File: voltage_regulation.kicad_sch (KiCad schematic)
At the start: 24 parts, among them IC3 NCV317BD2TR4G, U1 TPS73601MDRBREP, U2 TPS73601MDRBREP

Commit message: Lots of small changes
Some power and ground planes need to be looked at
All parts need to be reexamined before ordering
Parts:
- removed C21: 10uF, Capacitor_Tantalum_SMD:CP_EIA-7343-31_Kemet-D, symbol Device:C_Polarized
- removed C22: 10uF, Capacitor_SMD:C_1206_3216Metric, symbol Device:C_Small
- removed Cin1, Cin2: 1uF, Capacitor_SMD:C_1206_3216Metric, symbol Device:C_Polarized
- removed D1, D2: 1N4002, Diode_THT:D_DO-41_SOD81_P10.16mm_Horizontal, symbol Diode:1N4002
- removed IC3: NCV317BD2TR4G, SamacSys_Parts:TO254P1420X457-4N, symbol SamacSys_Parts:NCV317BD2TR4G
- removed RP1_1: 165, Resistor_SMD:R_0805_2012Metric, symbol Device:R
- removed RP1_2: 100, Resistor_SMD:R_0805_2012Metric, symbol Device:R
- added C71: 100uF, Capacitor_SMD:C_1206_3216Metric, symbol Device:C_Small
- added C72: 10nF, Capacitor_SMD:C_1206_3216Metric, symbol Device:C_Small
- added C73: 150pF, Capacitor_SMD:C_1206_3216Metric, symbol Device:C_Small
- added C74: 0.1uF, Capacitor_SMD:C_1206_3216Metric, symbol Device:C_Small
- added C75: 1500pF, Capacitor_SMD:C_1206_3216Metric, symbol Device:C_Small
- added C76, C77: 4.7uF, Capacitor_SMD:C_1206_3216Metric, symbol Device:C_Small
- added D1: MBRS340T3G, DIOM8059X261N, symbol SamacSys_Parts:MBRS340T3G
- added IC3: TPS5430DDAR, SOIC127P600X170-9N, symbol SamacSys_Parts:TPS5430DDAR
- added L1: SRP6060FA-150M, SRP6060FA150M, symbol SamacSys_Parts:SRP6060FA-150M
- added R10: 247k, Resistor_SMD:R_1206_3216Metric, symbol Device:R
- added R11: 33k, Resistor_SMD:R_1206_3216Metric, symbol Device:R
- added R7: 10k, Resistor_SMD:R_1206_3216Metric, symbol Device:R
- added R8: 5.9k, Resistor_SMD:R_1206_3216Metric, symbol Device:R
- added R9: 549, Resistor_SMD:R_1206_3216Metric, symbol Device:R
- U1, U2: value TPS73601MDRBREP -> TPS73601MDBVREP; Mouser Part Number 595-TPS73601MDRBREP -> 595-TPS73601MDBVREP; Mouser Price/Stock https://www.mouser.com/ProductDetail/Texas-Instruments/TPS73601MDRBREP?qs=IUbkBnfnSQLnzAa%252BAAvDVA%3D%3D -> https://www.mouser.com/ProductDetail/Texas-Instruments/TPS73601MDBVREP?qs=7kv20MEVUlgO8eFT%2FzKqZA%3D%3D
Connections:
- net +3V3: now also C71.1, C75.2, L1.2, R7.2
- net DC_LINE_IN_28V: now also C76.1, C77.1, IC3.7 (VIN), R10.1
- net GND: now also C71.2, C73.2, C76.2, C77.2, D1.2 (A), IC3.6 (GND), IC3.9 (EP), R11.2, R8.2, R9.2
- new net: C73.1, C74.1, C75.1, IC3.4 (VSENSE), R7.1, R8.1
- new net: C74.2, R9.1
- new net: C72.1, IC3.1 (BOOT)
- new net: C72.2, D1.1 (K), IC3.8 (PH), L1.1
- new net: IC3.5 (ENA), R10.2, R11.1
- no-connect marks 0 -> 3
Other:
- note removed: "NC"
- moved on the sheet: 2V1, 3V0, 3V3, C23, C24, C25, C26, C27, C28, RP2_1, RP2_2, RP3_1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

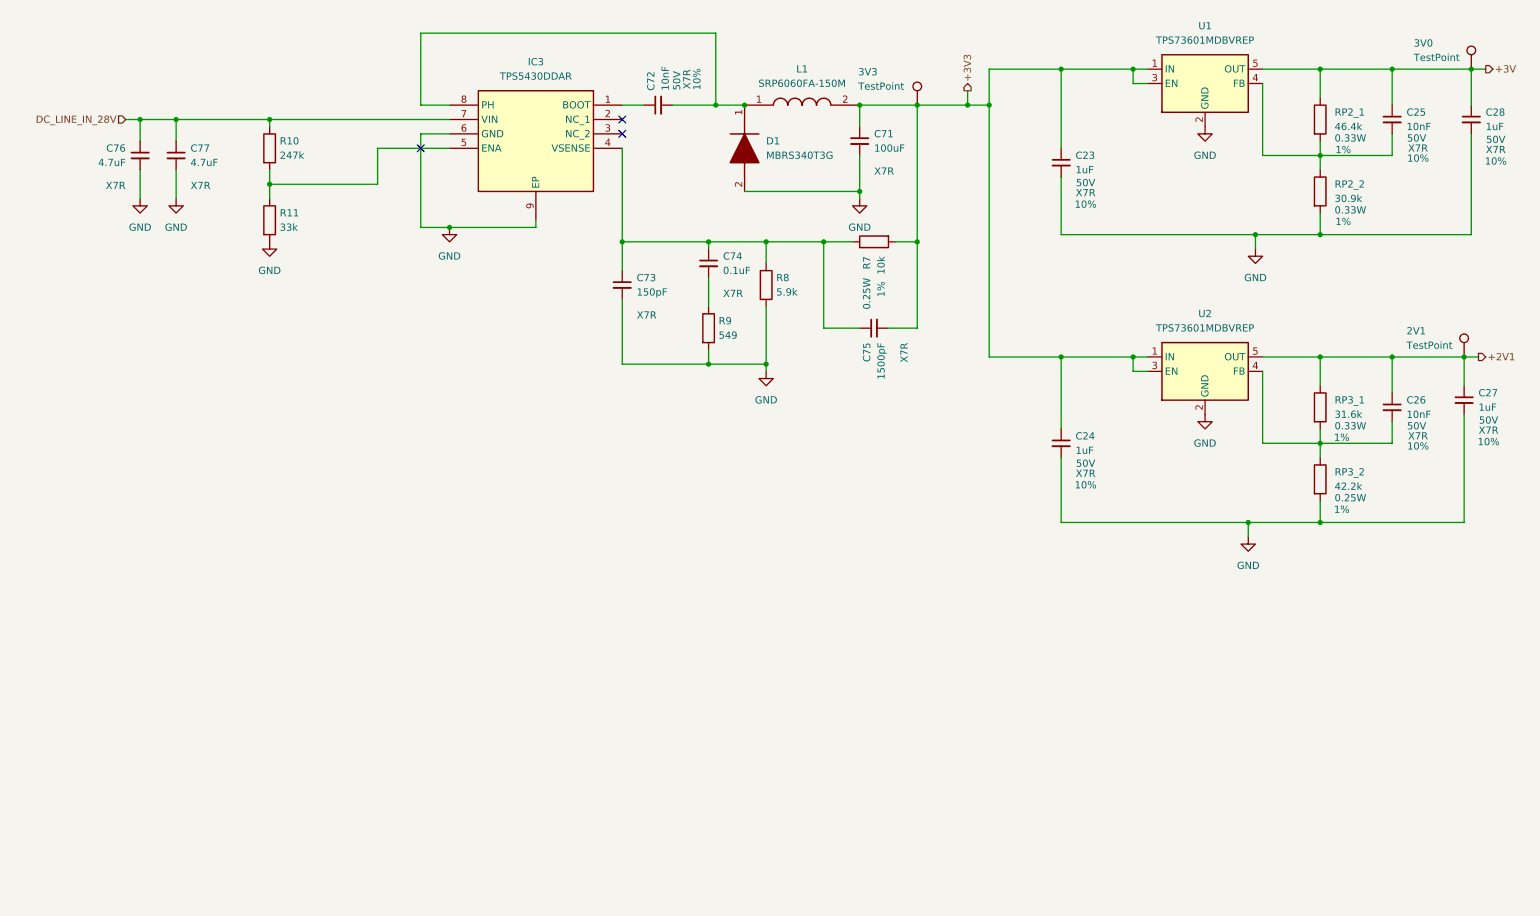
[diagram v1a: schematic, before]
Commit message: Almost done
Taking a break and making a push. Known things to do:
Add pull-up resistors to ETH MDIO, ETH MDC, and XRESL.
Source a 100uF capacitor for primary regulator.
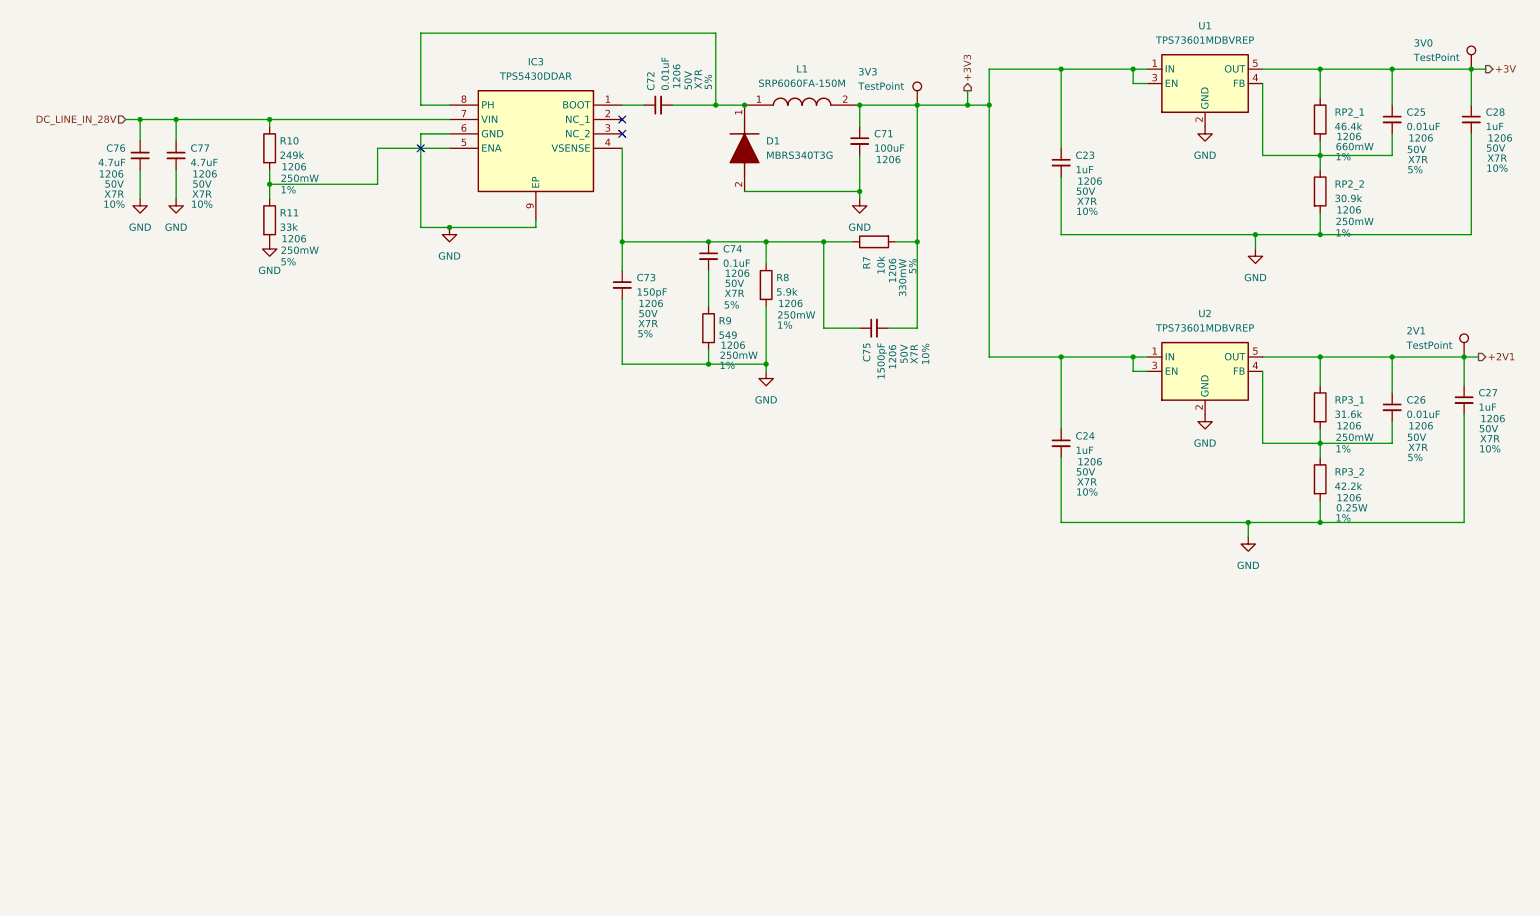
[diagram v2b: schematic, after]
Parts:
- C23, C24, C27, C28: footprint Capacitor_SMD:C_0603_1608Metric -> Capacitor_SMD:C_1206_3216Metric; Mouser Part Number 963-MLASU168AB7105KT -> 963-UMK316B7105KL-T; Mouser Price/Stock https://www.mouser.com/ProductDetail/TAIYO-YUDEN/MLASU168AB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 -> https://www.mouser.com/ProductDetail/TAIYO-YUDEN/UMK316B710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; Package Size (none) -> 1206
- C25, C26: value 10nF -> 0.01uF; footprint Capacitor_SMD:C_0603_1608Metric -> Capacitor_SMD:C_1206_3216Metric; Mouser Part Number 81-GCM188R71H103KA7J -> 581-12065C103J4T4A; Mouser Price/Stock https://www.mouser.com/ProductDetail/Murata-Electronics/GCM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 -> https://www.mouser.com/ProductDetail/KYOCERA-AVX/12065C103J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; Package Size (none) -> 1206; Tolerance 10% -> 5%
- C71: Dielectric X7R -> (none); Mouser Part Number (none) -> Multiple; Mouser Price/Stock (none) -> Multiple; Package Size (none) -> 1206
- C72: value 10nF -> 0.01uF; Mouser Part Number 81-GCM188R71H103KA7J -> 581-12065C103J4T4A; Mouser Price/Stock https://www.mouser.com/ProductDetail/Murata-Electronics/GCM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 -> https://www.mouser.com/ProductDetail/KYOCERA-AVX/12065C103J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; Package Size (none) -> 1206; Tolerance 10% -> 5%
- C73: Mouser Part Number (none) -> 80-C1206C151J5RACTU; Mouser Price/Stock (none) -> https://www.mouser.com/ProductDetail/KEMET/C1206C151J5RACTU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; Package Size (none) -> 1206; Tolerance (none) -> 5%; Voltage Rating (none) -> 50V
- C74: Mouser Part Number (none) -> 581-12065C104J4Z2A; Mouser Price/Stock (none) -> https://www.mouser.com/ProductDetail/KYOCERA-AVX/12065C104J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; Package Size (none) -> 1206; Tolerance (none) -> 5%; Voltage Rating (none) -> 50V
- C75: Mouser Part Number (none) -> 77-VJ1206Y152KXAAC; Mouser Price/Stock (none) -> https://www.mouser.com/ProductDetail/Vishay-Vitramon/VJ1206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; Package Size (none) -> 1206; Tolerance (none) -> 10%; Voltage Rating (none) -> 50V
- C76, C77: Mouser Part Number (none) -> 581-KGM31AR71H475KU; Mouser Price/Stock (none) -> https://www.mouser.com/ProductDetail/KYOCERA-AVX/KGM31AR71H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; Package Size (none) -> 1206; Tolerance (none) -> 10%; Voltage Rating (none) -> 50V
- IC3: Mouser Price/Stock https://www.mouser.co.uk/ProductDetail/Texas-Instruments/TP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 -> https://www.mouser.com/ProductDetail/Texas-Instruments/TPS5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
- R10: value 247k -> 249k; Mouser Part Number (none) -> 71-RCV1206249KFKEA; Mouser Price/Stock (none) -> https://www.mouser.com/ProductDetail/Vishay-Draloric/RCV120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; Package Size (none) -> 1206; Power Rating (none) -> 250mW; Tolerance (none) -> 1%
- R11: Mouser Part Number (none) -> 755-KTR18EZPJ333; Mouser Price/Stock (none) -> https://www.mouser.com/ProductDetail/ROHM-Semiconductor/KTR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; Package Size (none) -> 1206; Power Rating (none) -> 250mW; Tolerance (none) -> 5%
- R7: Mouser Part Number 71-CRCW060310K0FKEI -> 667-ERJ-T08J103V; Mouser Price/Stock https://www.mouser.com/ProductDetail/Vishay-Dale/CRCW060310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 -> https://www.mouser.com/ProductDetail/Panasonic/ERJ-T08J103V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; Package Size (none) -> 1206; Power Rating 0.25W -> 330mW; Tolerance 1% -> 5%
- R8: Mouser Part Number (none) -> 71-CRCW1206-5.9K-E3; Mouser Price/Stock (none) -> https://www.mouser.com/ProductDetail/Vishay-Dale/CRCW12065K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; Package Size (none) -> 1206; Power Rating (none) -> 250mW; Tolerance (none) -> 1%
- R9: Mouser Part Number (none) -> 71-CRCW1206-549-E3; Mouser Price/Stock (none) -> https://www.mouser.com/ProductDetail/Vishay-Dale/CRCW120654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; Package Size (none) -> 1206; Power Rating (none) -> 250mW; Tolerance (none) -> 1%
- RP2_1: footprint Resistor_SMD:R_0603_1608Metric -> Resistor_SMD:R_1206_3216Metric; Mouser Part Number 71-CRCW060346K4FKEAH -> 667-ERJ-P08F4642V; Mouser Price/Stock https://www.mouser.com/ProductDetail/Vishay-Dale/CRCW060346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 -> https://www.mouser.com/ProductDetail/Panasonic/ERJ-P08F4642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; Package Size (none) -> 1206; Power Rating 0.33W -> 660mW
- RP2_2: footprint Resistor_SMD:R_0603_1608Metric -> Resistor_SMD:R_1206_3216Metric; Mouser Part Number 71-CRCW060330K9FKEAH -> 652-CR1206FX-3092ELF; Mouser Price/Stock https://www.mouser.com/ProductDetail/Vishay-Dale/CRCW060330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 -> https://www.mouser.com/ProductDetail/Bourns/CR1206-FX-3092E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; Package Size (none) -> 1206; Power Rating 0.33W -> 250mW
- RP3_1: footprint Resistor_SMD:R_0603_1608Metric -> Resistor_SMD:R_1206_3216Metric; Mouser Part Number 71-CRCW060331K6FKEAH -> 71-CRCW120631K6FKEAC; Mouser Price/Stock https://www.mouser.com/ProductDetail/Vishay-Dale/CRCW060331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 -> https://www.mouser.com/ProductDetail/Vishay-Dale/CRCW120631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; Package Size (none) -> 1206; Power Rating 0.33W -> 250mW
- RP3_2: footprint Resistor_SMD:R_0603_1608Metric -> Resistor_SMD:R_1206_3216Metric; Mouser Part Number 71-RCS060342K2FKEA -> 71-CRCW1206-42.2K; Mouser Price/Stock https://www.mouser.com/ProductDetail/Vishay-Dale/RCS060342K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 -> https://www.mouser.com/ProductDetail/Vishay-Dale/CRCW120642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; Package Size (none) -> 1206
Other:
- moved on the sheet: C74

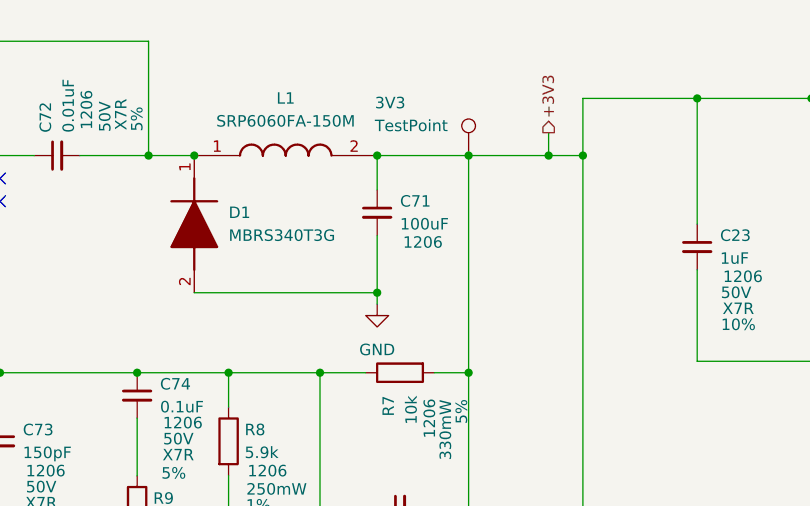
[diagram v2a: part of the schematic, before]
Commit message: Labeled test pads; marked tantalums with lines for cathode; found suitable tantalum for 100 uF
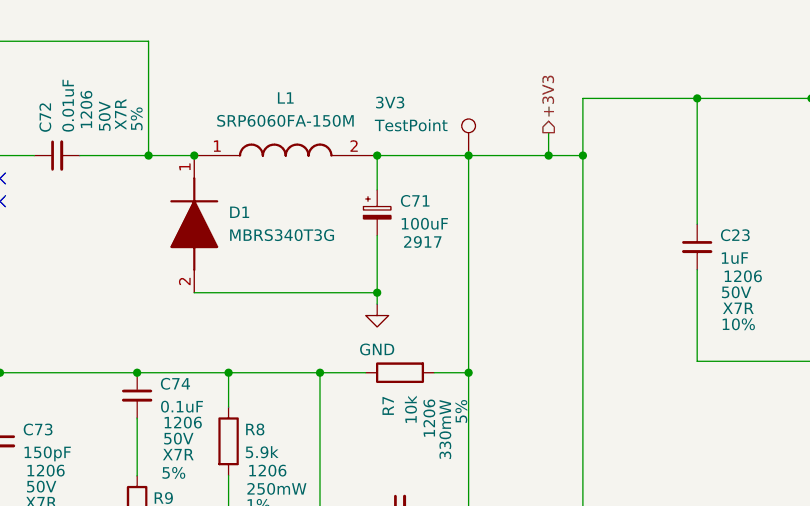
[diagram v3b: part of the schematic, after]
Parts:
- C71: footprint Capacitor_SMD:C_1206_3216Metric -> Capacitor_Tantalum_SMD:CP_EIA-7343-15_Kemet-W; symbol Device:C_Small -> Device:C_Polarized_Small; Mouser Part Number Multiple -> 74-293D107X9010D2TE3; Mouser Price/Stock Multiple -> 0.71/103,354; Package Size 1206 -> 2917
- D1: footprint DIOM8059X261N -> SamacSys_Parts:DIOM8059X261N
- IC3: footprint SOIC127P600X170-9N -> SamacSys_Parts:SOIC127P600X170-9N
- L1: footprint SRP6060FA150M -> SamacSys_Parts:SRP6060FA150M
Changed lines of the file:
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@@
 	)
 	(symbol
-		(lib_id "Device:C_Small")
+		(lib_id "Device:C_Polarized_Small")
 		(at 163.83 38.1 0)
 		(unit 1)
@@
 			)
 		)
-		(property "Footprint" "Capacitor_SMD:C_1206_3216Metric"
+		(property "Footprint" "Capacitor_Tantalum_SMD:CP_EIA-7343-15_Kemet-W"
 			(at 163.83 38.1 0)
 			(effects
@@
 			)
 		)
-		(property "Description" "Unpolarized capacitor, small symbol"
+		(property "Description" "Polarized capacitor, small symbol"
 			(at 163.83 38.1 0)
 			(effects
@@
 			)
 		)
-		(property "Mouser Part Number" "Multiple"
+		(property "Mouser Part Number" " 74-293D107X9010D2TE3"
 			(at 163.83 38.1 0)
 			(effects
@@
 			)
 		)
-		(property "Mouser Price/Stock" "Multiple"
+		(property "Mouser Price/Stock" "0.71/103,354"
 			(at 163.83 38.1 0)
 			(effects
@@
 			)
 		)
-		(property "Package Size" "1206"
+		(property "Package Size" "2917"
 			(at 168.91 41.402 0)
 			(effects
@@
 			)
 		)
-		(property "Footprint" "SRP6060FA150M"
+		(property "Footprint" "SamacSys_Parts:SRP6060FA150M"
 			(at 160.02 127.94 0)
 			(effects
@@
 			)
 		)
-		(property "Footprint" "SOIC127P600X170-9N"
+		(property "Footprint" "SamacSys_Parts:SOIC127P600X170-9N"
 			(at 95.25 126.67 0)
 			(effects
@@
 			)
 		)
-		(property "Footprint" "DIOM8059X261N"
+		(property "Footprint" "SamacSys_Parts:DIOM8059X261N"
 			(at 46.05 43.18 0)
 			(effects
